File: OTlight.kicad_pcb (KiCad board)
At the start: 2 copper layers, 90 x 55 mm, 86 parts, among them P1 CONN_01X02, Q1 TEMT6000, Q2 RSR030N06TL, T1 TRANSFO, U1 LM3478, U10 IN-14, U11 IN-14, U12 MAX6931, U13 IN-14, U14 MAX6920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

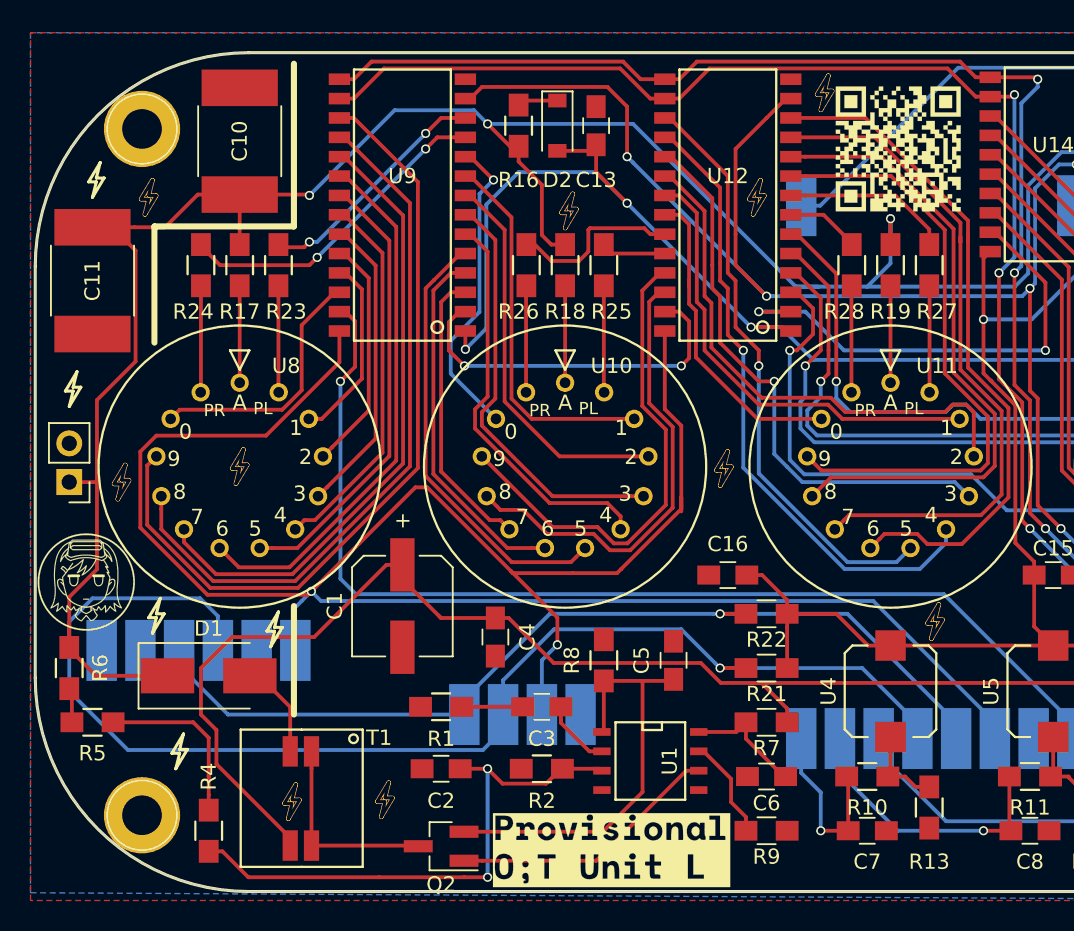
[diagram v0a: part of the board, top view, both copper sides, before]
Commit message: Changed QR code for non inverted colours Moved Q2 silkscreen Changed Biri-Biri via for 0.3mm
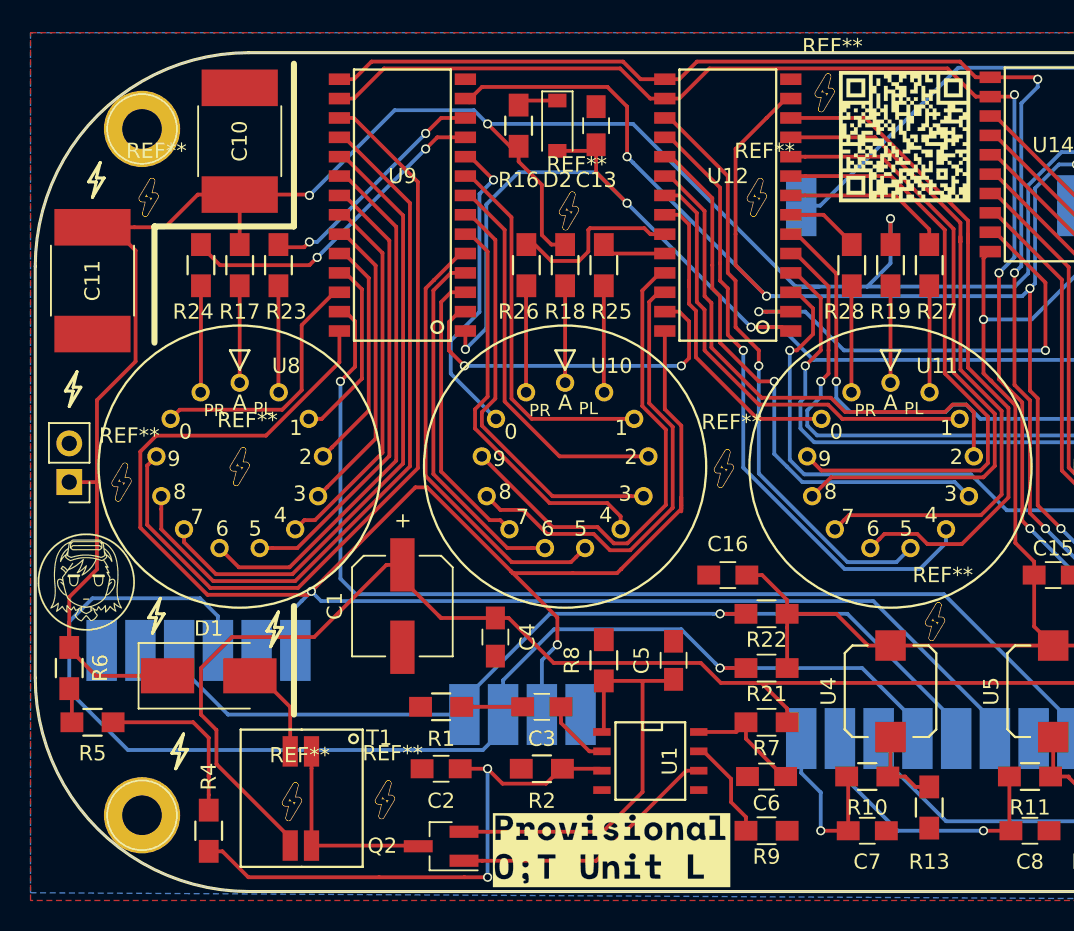
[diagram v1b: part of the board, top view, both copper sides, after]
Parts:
- removed the G*** at (100.6, 83.3)
- added G***: LOGO, BamboulabFootprints:QRcodeOTL, F.Cu at (101.0, 82.5)

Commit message: Rev2 of the board Everything fits and is connected~
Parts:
- removed the ? at (127.0, 82.0)
- removed the ? at (51.0, 127.0)
- removed the ? at (51.0, 82.0)
- removed the ? at (127.0, 127.0)
- removed R24, R25, R26, R27, R28, R29, R30: R_Small, Resistors_SMD:R_0805_HandSoldering
- removed REF** (x11): Biri-Biri via, BamboulabFootprints:Biri-Biri-via-small
- removed U10, U11, U13, U8: IN-14, BamboulabFootprints:IN-14
- added C17: C_Small, Capacitors_SMD:C_0805_HandSoldering, F.Cu at (113.5, 112.3)
- added C18: 0.1u, Capacitors_SMD:C_0805_HandSoldering, F.Cu at (123.2, 123.2)
- added P2: CONN_01X14, Pin_Headers:Pin_Header_Straight_2x07_Pitch1.27mm, F.Cu at (57.5, 108.0)
- added P3: CONN_01X14, Pin_Headers:Pin_Header_Straight_2x07_Pitch1.27mm, F.Cu at (78.9, 108.0)
- added P4: CONN_01X14, Pin_Headers:Pin_Header_Straight_2x07_Pitch1.27mm, F.Cu at (100.2, 108.0)
- added P5: CONN_01X14, Pin_Headers:Pin_Header_Straight_2x07_Pitch1.27mm, F.Cu at (121.5, 108.0)
- U2: footprint BamboulabFootprints:NodeMCU-V3 -> BamboulabFootprints:NodeMCU-V2
- U3: footprint BamboulabFootprints:DS3231-Angled -> BamboulabFootprints:DS3231; moved to F.Cu
- U7: value BME280 -> bareBME280; footprint BamboulabFootprints:BME280-Angled -> BamboulabFootprints:BME280bare; moved to F.Cu
- moved R17 84.2 mm to (123.1, 143.5), turned to 0 degrees
- moved U7 74.9 mm to (127.6, 123.8), turned to 0 degrees
- moved R23 73.4 mm to (123.2, 128.3)
- moved C14 66.2 mm to (65.0, 115.6), turned to 0 degrees
- moved G*** 63.6 mm to (73.9, 192.4)
- moved R18 59.4 mm to (111.8, 140.3), turned to 0 degrees
- moved R19 58.2 mm to (118.7, 146.1), turned to 0 degrees
- moved G*** 53.6 mm to (119.3, 32.1)
- moved Q2 49.7 mm to (62.2, 80.0), turned to 0 degrees
- moved R20 48.9 mm to (117.4, 139.7), turned to 0 degrees
- moved T1 46.7 mm to (76.8, 81.9), turned to 180 degrees
- moved D1 46.1 mm to (85.1, 82.5), turned to 90 degrees
- moved R7 46.0 mm to (68.6, 81.3)
- moved C6 45.8 mm to (68.6, 85.1), turned to 0 degrees
- moved R9 45.6 mm to (68.6, 88.9)
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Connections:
- D2 pad 1: Net-(D2-Pad1) -> GND
- R16 pad 2: Net-(D2-Pad1) -> Net-(C12-Pad2)
- R17 pad 1: /HVout -> Net-(R17-Pad1)
- R18 pad 1: /HVout -> Net-(R18-Pad1)
- R19 pad 1: /HVout -> Net-(R19-Pad1)
- R20 pad 1: /HVout -> Net-(R20-Pad1)
- R23 pad 2: Net-(R23-Pad2) -> +3V3
- U12 pad 13: /BLANK -> GND
- U14 pad 9: /BLANK -> GND
- U2 pad 20: /BLANK -> Net-(C9-Pad1)
- U2 pad 28: Net-(C9-Pad1) -> Net-(C8-Pad1)
- U2 pad 29: Net-(C8-Pad1) -> Net-(C7-Pad1)
- U2 pad 30: Net-(C7-Pad1) -> Net-(U2-Pad30)
- U7 pad 1: +3V3 -> GND
- U7 pad 2: GND -> +3V3
- U7 pad 5: Net-(U7-Pad5) -> Net-(R23-Pad1)
- U7 pad 6: Net-(U7-Pad6) -> +3V3
- U9 pad 12: Net-(R23-Pad2) -> Net-(P2-Pad11)
- U9 pad 13: /BLANK -> GND
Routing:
- net +3V3: track 278.8 -> 132.7 mm, vias 4 -> 0
- net /BLANK: track 111.4 -> 0.00 mm, vias 5 -> 0
- net /HVout: track 156.9 -> 93.1 mm, vias 4 -> 0
- net +5V: track 131.0 -> 71.5 mm, vias 1 -> 2
- net Net-(P2-Pad9): track 46.7 -> 5.89 mm
- net Net-(P4-Pad8): track 44.6 -> 8.81 mm, vias 0 -> 1
- net Net-(P4-Pad10): track 40.5 -> 4.84 mm, vias 0 -> 1
- net Net-(Q1-Pad2): track 33.9 -> 0.00 mm, vias 1 -> 0
- net Net-(R22-Pad2): track 63.3 -> 96.0 mm, vias 1 -> 0
- net Net-(P2-Pad7): track 35.4 -> 5.36 mm
- net Net-(P4-Pad9): track 42.1 -> 12.2 mm, vias 0 -> 1
- net Net-(P2-Pad10): track 53.1 -> 27.6 mm, vias 0 -> 1
- net /CLK: track 95.6 -> 72.5 mm
- net Net-(C9-Pad1): track 25.0 -> 2.48 mm, vias 1 -> 0
- net /LOAD: track 93.2 -> 71.5 mm
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- removed copper zone on B.Cu, net GND
- removed copper zone on F.Cu, net GND
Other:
- board outline removed
- net class Default: clearance 0.2 -> 0.15
- rule trace_clearance: 0.2 -> 0.15

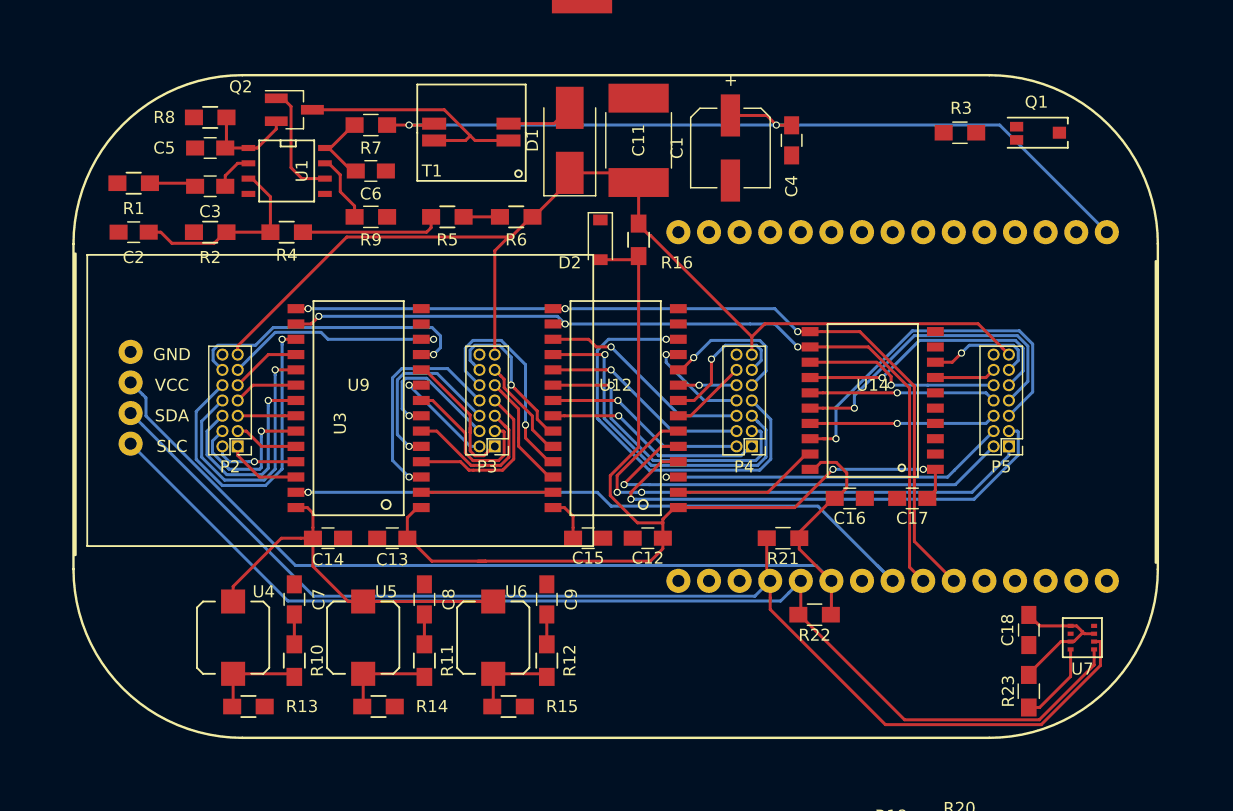
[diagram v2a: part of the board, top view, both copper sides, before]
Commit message: Added edge cut and M3 mounting holes
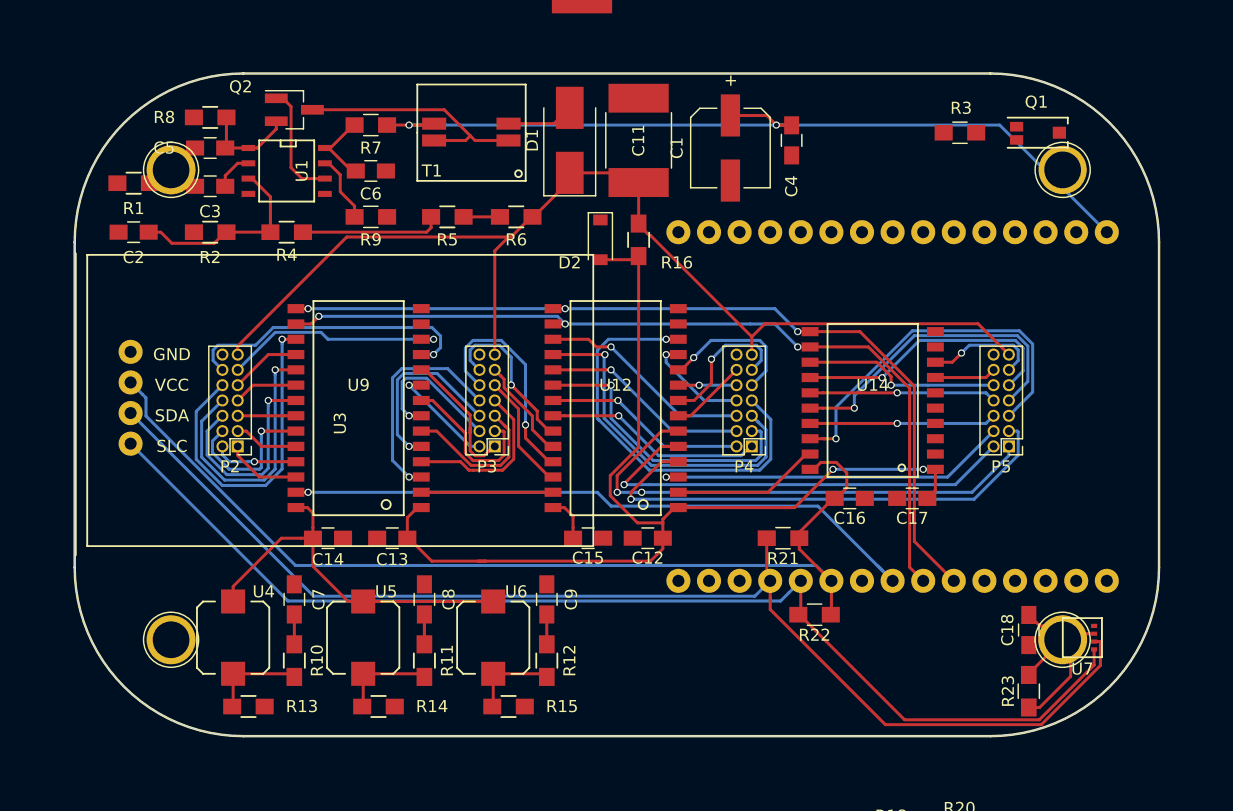
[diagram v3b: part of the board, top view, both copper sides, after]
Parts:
- added REF**: 1pin, Connectors:1pin, F.Cu at (126.0, 85.0)
- added REF**: 1pin, Connectors:1pin, F.Cu at (52.0, 85.0)
- added REF**: 1pin, Connectors:1pin, F.Cu at (126.0, 124.0)
- added REF**: 1pin, Connectors:1pin, F.Cu at (52.0, 124.0)
- moved ? 0.17 mm to (89.0, 104.0)
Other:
- board outline added: 90 x 55 mm
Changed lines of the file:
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@@
-(kicad_pcb (version 4) (host pcbnew 4.0.5)
+(kicad_pcb (version 4) (host pcbnew 4.0.6)
   (general
-    (links 179)
-    (no_connects 109)
-    (area 0 0 0 0)
+    (links 0)
+    (no_connects 56)
+    (area 20.416667 27.674387 148.483921 194.98277)
     (thickness 1.6)
-    (drawings 12)
+    (drawings 19)
     (tracks 618)
     (zones 0)
-    (modules 66)
+    (modules 70)
     (nets 109)
   )
@@
     (mod_text_size 1 1)
     (mod_text_width 0.15)
-    (pad_size 1.73 0.4)
-    (pad_drill 1.63)
+    (pad_size 4 4)
+    (pad_drill 3.048)
     (pad_to_mask_clearance 0)
     (aux_axis_origin 0 0)
@@
   )
   (module BamboulabFootprints:Altoid locked (layer F.Cu)
-    (at 88.9 104.14)
+    (at 89 104)
     (attr virtual)
     (fp_text reference "" (at 0 5.08) (layer F.SilkS)
@@
       (net 13 +3V3))
   )
+  (module Connectors:1pin locked (layer F.Cu)
+    (at 126 85)
+    (descr "module 1 pin (ou trou mecanique de percage)")
+    (tags DEV)
+    (fp_text reference REF** (at 0 -3.048) (layer F.SilkS) hide
+      (effects (font (size 1 1) (thickness 0.15)))
+    )
+    (fp_text value 1pin (at 0 3) (layer F.Fab)
+      (effects (font (size 1 1) (thickness 0.15)))
+    )
+    (fp_circle (center 0 0) (end 2 0.8) (layer F.Fab) (width 0.1))
+    (fp_circle (center 0 0) (end 2.6 0) (layer F.CrtYd) (width 0.05))
+    (fp_circle (center 0 0) (end 0 -2.286) (layer F.SilkS) (width 0.12))
+    (pad 1 thru_hole circle (at 0 0) (size 4 4) (drill 3.048) (layers *.Cu *.Mask))
+  )
+  (module Connectors:1pin locked (layer F.Cu)
+    (at 52 85)
+    (descr "module 1 pin (ou trou mecanique de percage)")
+    (tags DEV)
+    (fp_text reference REF** (at 0 -3.048) (layer F.SilkS) hide
+      (effects (font (size 1 1) (thickness 0.15)))
+    )
+    (fp_text value 1pin (at 0 3) (layer F.Fab)
+      (effects (font (size 1 1) (thickness 0.15)))
+    )
+    (fp_circle (center 0 0) (end 2 0.8) (layer F.Fab) (width 0.1))
+    (fp_circle (center 0 0) (end 2.6 0) (layer F.CrtYd) (width 0.05))
+    (fp_circle (center 0 0) (end 0 -2.286) (layer F.SilkS) (width 0.12))
+    (pad 1 thru_hole circle (at 0 0) (size 4.064 4.064) (drill 3.048) (layers *.Cu *.Mask))
+  )
+  (module Connectors:1pin locked (layer F.Cu)
+    (at 126 124)
+    (descr "module 1 pin (ou trou mecanique de percage)")
+    (tags DEV)
+    (fp_text reference REF** (at 0 -3.048) (layer F.SilkS) hide
+      (effects (font (size 1 1) (thickness 0.15)))
+    )
+    (fp_text value 1pin (at 0 3) (layer F.Fab)
+      (effects (font (size 1 1) (thickness 0.15)))
+    )
+    (fp_circle (center 0 0) (end 2 0.8) (layer F.Fab) (width 0.1))
+    (fp_circle (center 0 0) (end 2.6 0) (layer F.CrtYd) (width 0.05))
+    (fp_circle (center 0 0) (end 0 -2.286) (layer F.SilkS) (width 0.12))
+    (pad 1 thru_hole circle (at 0 0) (size 4.064 4.064) (drill 3.048) (layers *.Cu *.Mask))
+  )
+  (module Connectors:1pin locked (layer F.Cu)
+    (at 52 124)
+    (descr "module 1 pin (ou trou mecanique de percage)")
+    (tags DEV)
+    (fp_text reference REF** (at 0 -3.048) (layer F.SilkS) hide
+      (effects (font (size 1 1) (thickness 0.15)))
+    )
+    (fp_text value 1pin (at 0 3) (layer F.Fab)
+      (effects (font (size 1 1) (thickness 0.15)))
+    )
+    (fp_circle (center 0 0) (end 2 0.8) (layer F.Fab) (width 0.1))
+    (fp_circle (center 0 0) (end 2.6 0) (layer F.CrtYd) (width 0.05))
+    (fp_circle (center 0 0) (end 0 -2.286) (layer F.SilkS) (width 0.12))
+    (pad 1 thru_hole circle (at 0 0) (size 4.064 4.064) (drill 3.048) (layers *.Cu *.Mask))
+  )
+  (gr_arc (start 58 91) (end 44 91) (angle 90) (layer Edge.Cuts) (width 0.1))
+  (gr_arc (start 58 118) (end 58 132) (angle 90) (layer Edge.Cuts) (width 0.1))
+  (gr_arc (start 120 118) (end 134 118) (angle 90) (layer Edge.Cuts) (width 0.1))
+  (gr_arc (start 120 91) (end 120 77) (angle 90) (layer Edge.Cuts) (width 0.1))
+  (gr_line (start 58 77) (end 120 77) (layer Edge.Cuts) (width 0.1))
+  (gr_line (start 44 118) (end 44 91) (layer Edge.Cuts) (width 0.1))
+  (gr_line (start 120 132) (end 58 132) (layer Edge.Cuts) (width 0.1))
+  (gr_line (start 134 91) (end 134 118) (layer Edge.Cuts) (width 0.1))
   (gr_line (start 44.069 91.948) (end 44.069 116.967) (layer F.SilkS) (width 0.2))
-  (gr_line (start 133.731 92.583) (end 133.731 117.602) (layer F.SilkS) (width 0.2))
   (gr_line (start 26.162 97.917) (end 25.4 99.187) (layer F.SilkS) (width 0.2))
   (gr_line (start 25.654 98.171) (end 25.146 98.171) (layer F.SilkS) (width 0.2))
